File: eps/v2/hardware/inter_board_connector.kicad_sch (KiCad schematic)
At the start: 1 part, among them J1 Conn_02x20_Odd_Even

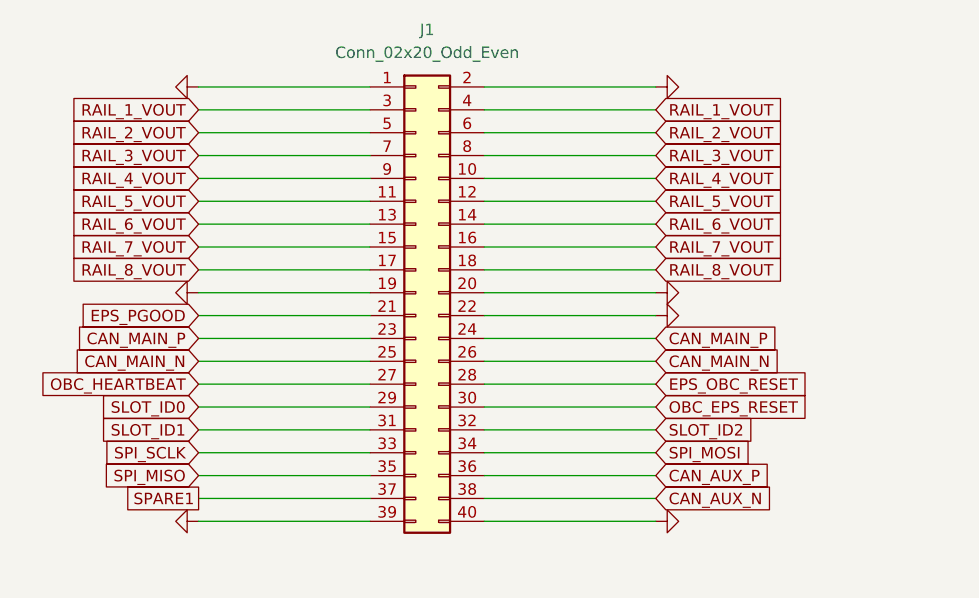
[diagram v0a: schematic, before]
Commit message: revise mux & create skeleton
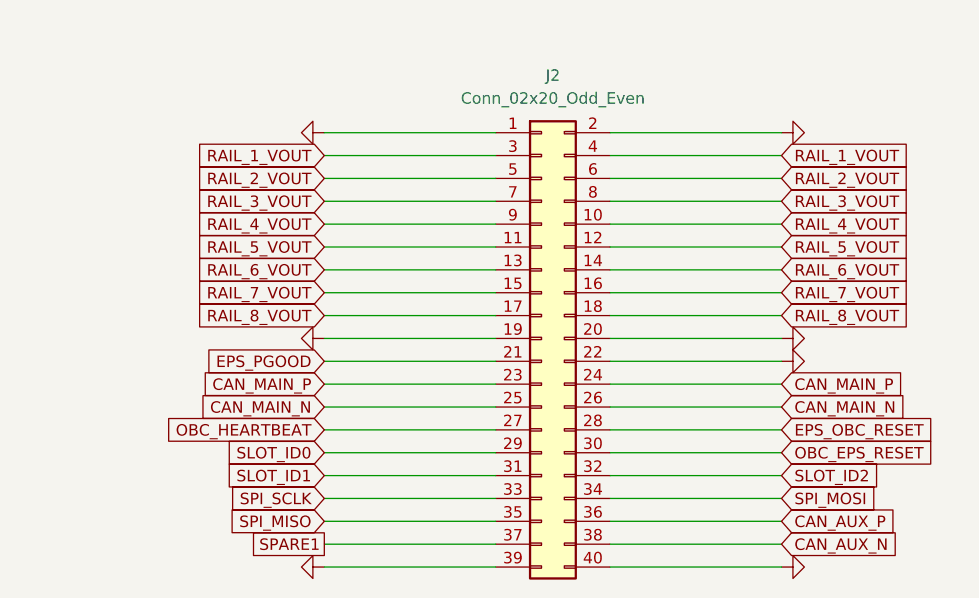
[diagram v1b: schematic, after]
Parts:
- renumbered J1 to J2
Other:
- moved on the sheet: J2
